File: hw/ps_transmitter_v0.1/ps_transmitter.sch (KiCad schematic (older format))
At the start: 7 parts, among them SW1 SW_SCANC, SW2 SW_FN, U1 WeMos_D1_mini, U2 oled1.3, U3 Intrasense_calib_board

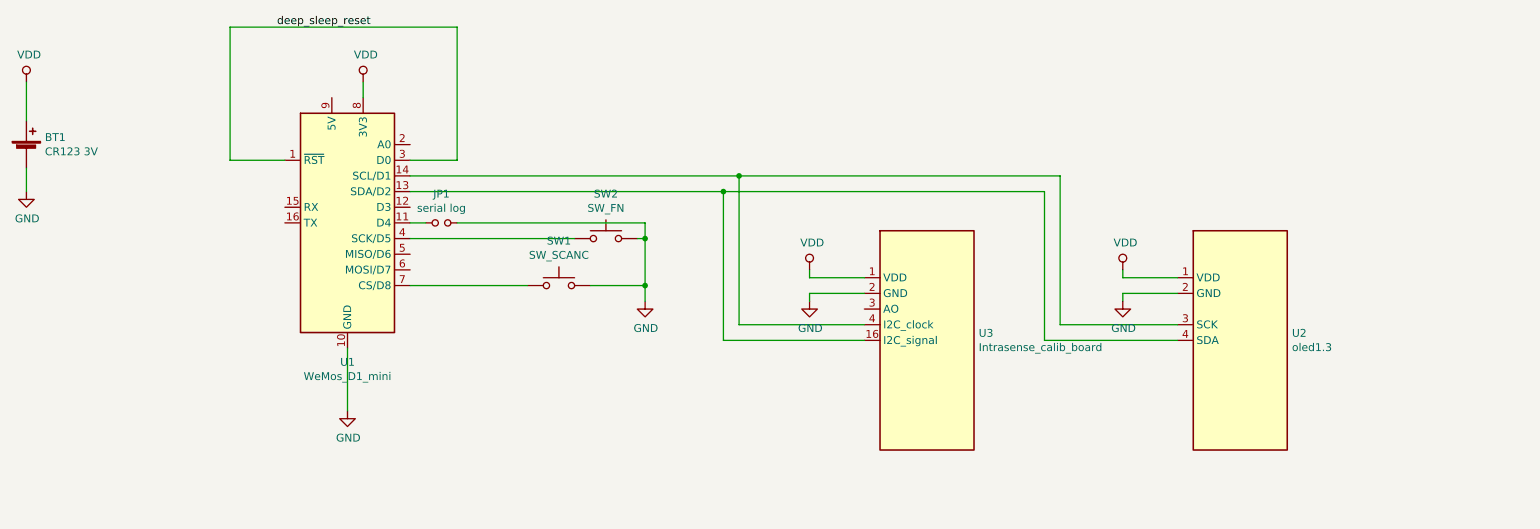
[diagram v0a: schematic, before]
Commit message: Inclusion placa fuente en V0.1
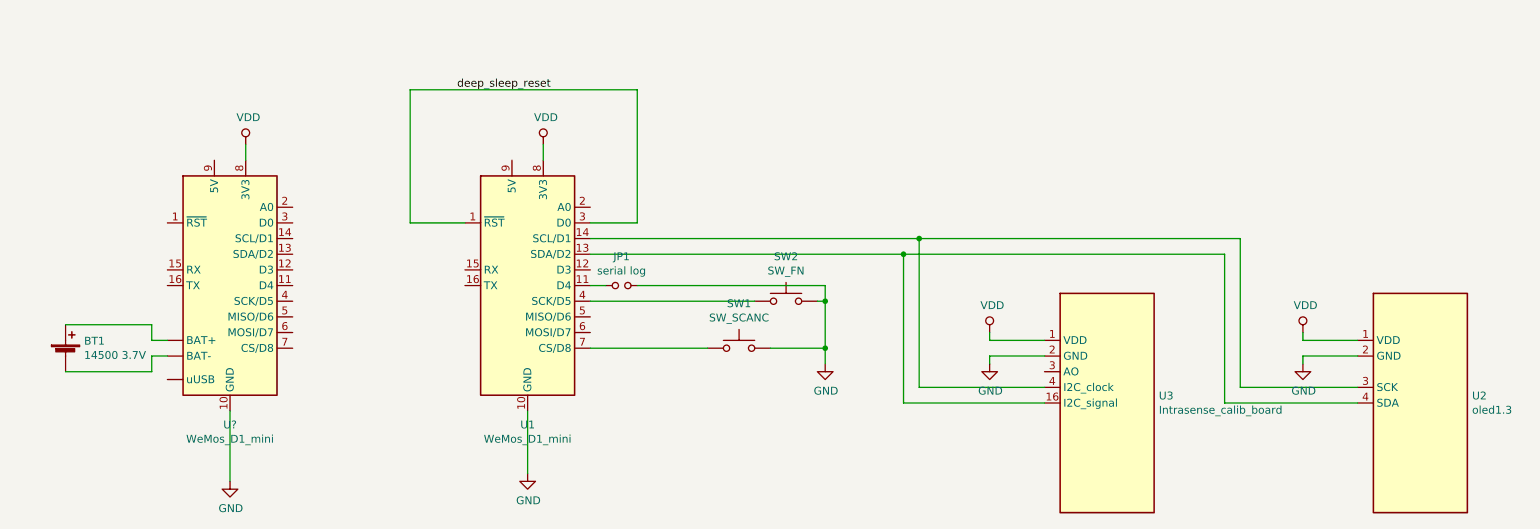
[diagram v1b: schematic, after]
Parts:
- added U?: WeMos_D1_mini, Module:WEMOS_D1_mini_light, symbol wemos_d1_mini_batery_shield:WeMos_D1_mini
- BT1: value CR123 3V -> 14500 3.7V
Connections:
- net GND: now also U?.10 (GND); no longer BT1.2 (-)
- net VDD: now also U?.8 (3V3); no longer BT1.1 (+)
- new net: BT1.1 (+), U?.~ (uUSB)
- new net: BT1.2 (-), U?.~ (uUSB)
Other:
- moved on the sheet: BT1, JP1, SW1, SW2, U1, U2, U3
